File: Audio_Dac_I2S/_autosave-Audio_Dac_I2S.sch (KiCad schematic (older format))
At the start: 35 parts

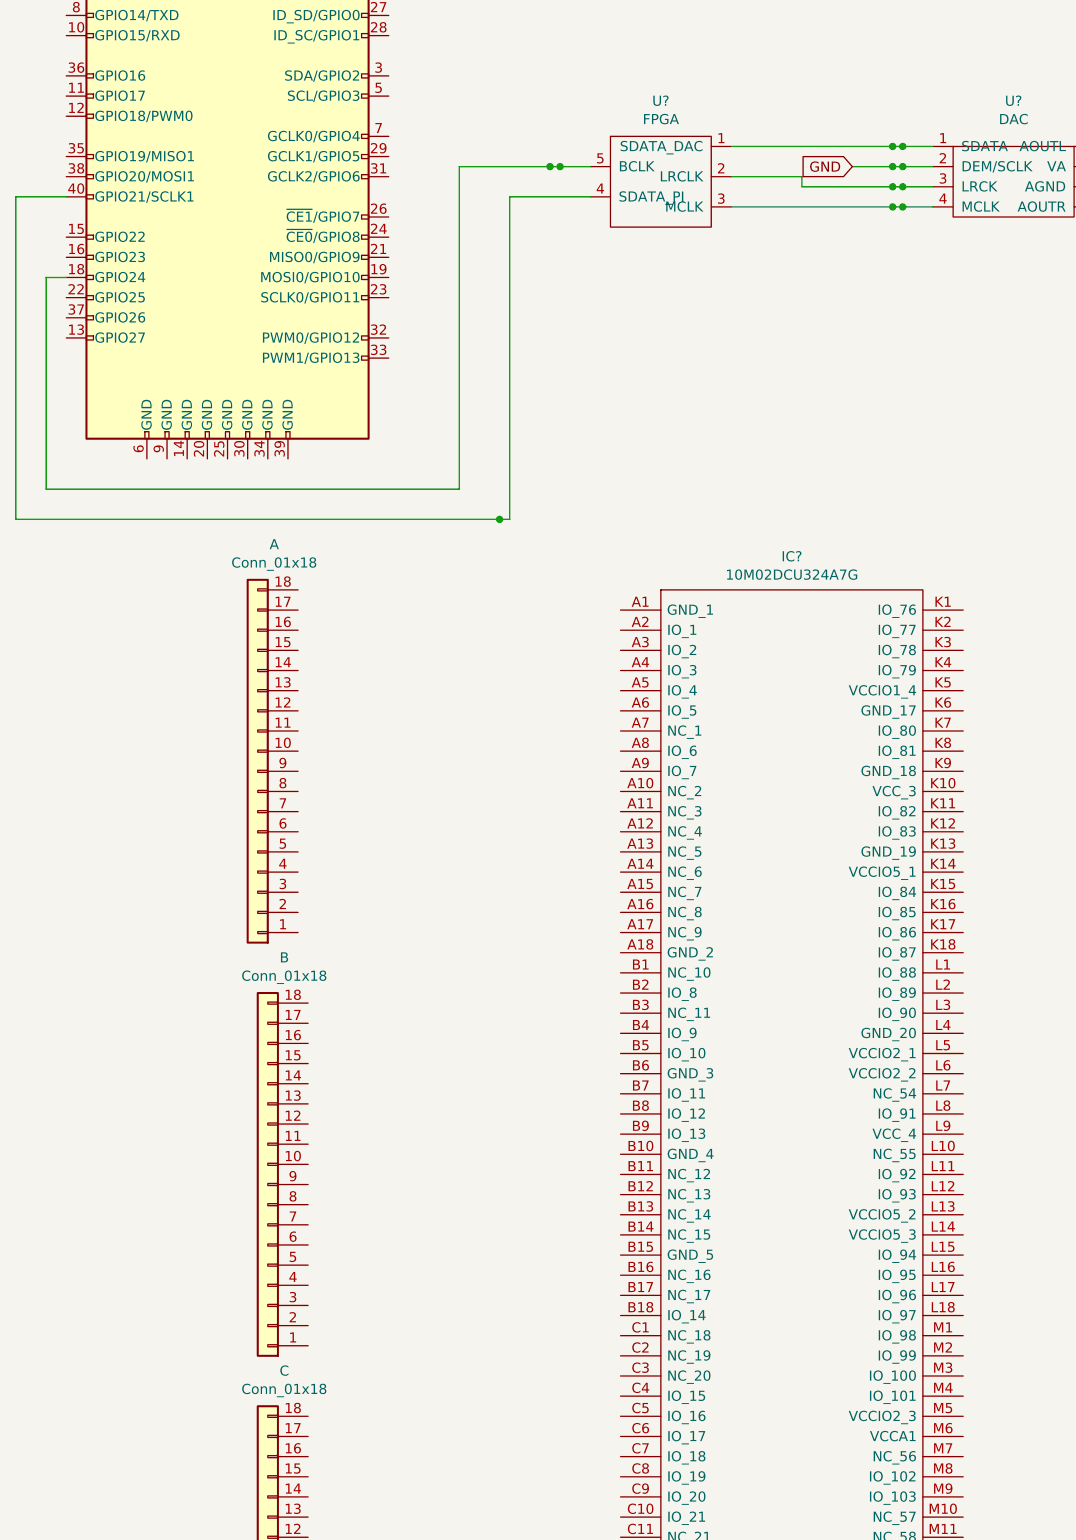
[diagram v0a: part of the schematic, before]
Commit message: updated schematics and footprints
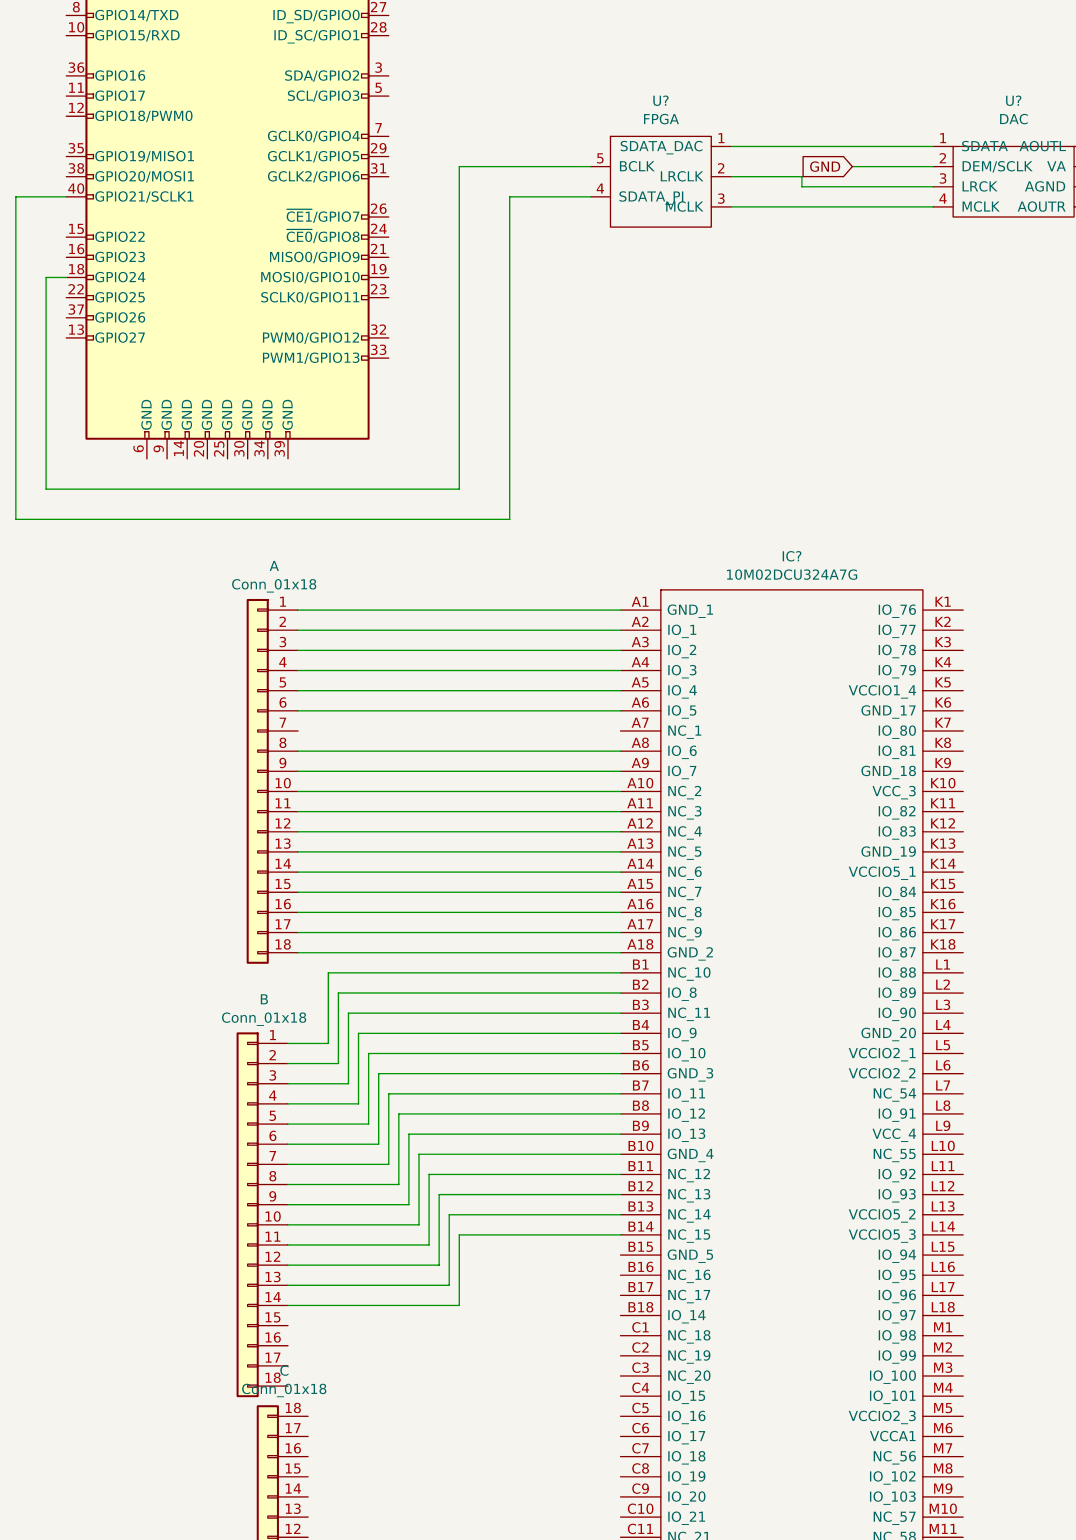
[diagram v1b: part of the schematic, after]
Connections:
- net at IC?.A1 (GND_1): now also A.1 (Pin_1)
- net at IC?.A10 (NC_2): now also A.10 (Pin_10)
- net at IC?.A11 (NC_3): now also A.11 (Pin_11)
- net at IC?.A12 (NC_4): now also A.12 (Pin_12)
- net at IC?.A13 (NC_5): now also A.13 (Pin_13)
- net at IC?.A14 (NC_6): now also A.14 (Pin_14)
- net at IC?.A15 (NC_7): now also A.15 (Pin_15)
- net at IC?.A16 (NC_8): now also A.16 (Pin_16)
- net at IC?.A17 (NC_9): now also A.17 (Pin_17)
- net at IC?.A18 (GND_2): now also A.18 (Pin_18)
- net at IC?.A2 (IO_1): now also A.2 (Pin_2)
- net at IC?.A3 (IO_2): now also A.3 (Pin_3)
- net at IC?.A4 (IO_3): now also A.4 (Pin_4)
- net at IC?.A5 (IO_4): now also A.5 (Pin_5)
- net at IC?.A6 (IO_5): now also A.6 (Pin_6)
- net at IC?.A8 (IO_6): now also A.8 (Pin_8)
- net at IC?.A9 (IO_7): now also A.9 (Pin_9)
- net at IC?.B1 (NC_10): now also B.1 (Pin_1)
- net at IC?.B10 (GND_4): now also B.10 (Pin_10)
- net at IC?.B11 (NC_12): now also B.11 (Pin_11)
- net at IC?.B12 (NC_13): now also B.12 (Pin_12)
- net at IC?.B13 (NC_14): now also B.13 (Pin_13)
- net at IC?.B14 (NC_15): now also B.14 (Pin_14)
- net at IC?.B2 (IO_8): now also B.2 (Pin_2)
- net at IC?.B3 (NC_11): now also B.3 (Pin_3)
- net at IC?.B4 (IO_9): now also B.4 (Pin_4)
- net at IC?.B5 (IO_10): now also B.5 (Pin_5)
- net at IC?.B6 (GND_3): now also B.6 (Pin_6)
- net at IC?.B7 (IO_11): now also B.7 (Pin_7)
- net at IC?.B8 (IO_12): now also B.8 (Pin_8)
- net at IC?.B9 (IO_13): now also B.9 (Pin_9)
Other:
- moved on the sheet: A, B
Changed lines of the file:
@@
 Text GLabel 4900 3400 0    50   Input ~ 0
 GND
-Wire Wire Line
-	5300 3400 5150 3400
 $Comp
 L CustomLib:FPGA U?
@@
 $EndComp
 Wire Wire Line
-	4300 3600 5100 3600
-Wire Wire Line
 	4300 3450 4650 3450
 Wire Wire Line
 	4650 3450 4650 3500
-Wire Wire Line
-	4650 3500 5100 3500
-Wire Wire Line
-	4300 3300 5100 3300
 $Comp
 L Connector:Raspberry_Pi_2_3 J?
@@
 	750  3550 750  5150
 Wire Wire Line
-	750  5150 3150 5150
-Wire Wire Line
 	3200 5150 3200 3550
 Wire Wire Line
@@
 Wire Wire Line
 	2950 5000 2950 3400
-Wire Wire Line
-	2950 3400 3400 3400
 Wire Wire Line
 	8100 4800 9200 4800
@@
 	1    0    0    -1
 $EndComp
-Connection ~ 3450 3400
-Wire Wire Line
-	3450 3400 3600 3400
-Connection ~ 5150 3300
-Wire Wire Line
-	5150 3300 5300 3300
-Connection ~ 5150 3400
-Wire Wire Line
-	5150 3400 5100 3400
-Connection ~ 5150 3500
-Wire Wire Line
-	5150 3500 5300 3500
-Connection ~ 5150 3600
-Wire Wire Line
-	5150 3600 5300 3600
-Connection ~ 3400 3400
-Wire Wire Line
-	3400 3400 3450 3400
-Connection ~ 5100 3300
-Wire Wire Line
-	5100 3300 5150 3300
-Connection ~ 5100 3400
-Wire Wire Line
-	5100 3400 4900 3400
-Connection ~ 5100 3500
-Wire Wire Line
-	5100 3500 5150 3500
-Connection ~ 5100 3600
-Wire Wire Line
-	5100 3600 5150 3600
-Connection ~ 3150 5150
-Wire Wire Line
-	3150 5150 3200 5150
-$Comp
-L Connector_Generic:Conn_01x18 A
-U 1 1 6195A7F2
-P 1950 6400
-F 0 "A" H 1868 5275 50  0000 C CNN
-F 1 "Conn_01x18" H 1868 5366 50  0000 C CNN
-F 2 "" H 1950 6400 50  0001 C CNN
-F 3 "~" H 1950 6400 50  0001 C CNN
-	1    1950 6400
-	-1   0    0    1
-$EndComp
 $Comp
 L Connector_Generic:Conn_01x18 B
 U 1 1 6195C231
-P 2000 8450
-F 0 "B" H 1918 7325 50  0000 C CNN
-F 1 "Conn_01x18" H 1918 7416 50  0000 C CNN
-F 2 "" H 2000 8450 50  0001 C CNN
-F 3 "~" H 2000 8450 50  0001 C CNN
-	1    2000 8450
-	-1   0    0    1
+P 1900 8550
+F 0 "B" H 1818 9567 50  0000 C CNN
+F 1 "Conn_01x18" H 1818 9476 50  0000 C CNN
+F 2 "" H 1900 8550 50  0001 C CNN
+F 3 "~" H 1900 8550 50  0001 C CNN
+	1    1900 8550
+	-1   0    0    -1
 $EndComp
 $Comp
@@
 	1    0    0    -1
 $EndComp
+$Comp
+L Connector_Generic:Conn_01x18 A
+U 1 1 6195A7F2
+P 1950 6400
+F 0 "A" H 1868 7417 50  0000 C CNN
+F 1 "Conn_01x18" H 1868 7326 50  0000 C CNN
+F 2 "" H 1950 6400 50  0001 C CNN
+F 3 "~" H 1950 6400 50  0001 C CNN
+	1    1950 6400
+	-1   0    0    -1
+$EndComp
+Wire Wire Line
+	2950 3400 3600 3400
+Wire Wire Line
+	750  5150 3200 5150
+Wire Wire Line
+	4300 3300 5300 3300
+Wire Wire Line
+	4650 3500 5300 3500
+Wire Wire Line
+	4300 3600 5300 3600
+Wire Wire Line
+	4900 3400 5300 3400
+Wire Wire Line
+	2150 5600 3750 5600
+Wire Wire Line
+	3750 5700 2150 5700
+Wire Wire Line
+	2150 5800 3750 5800
+Wire Wire Line
+	3750 5900 2150 5900
+Wire Wire Line
+	2150 6000 3750 6000
+Wire Wire Line
+	3750 6100 2150 6100
+Wire Wire Line
+	2150 6300 3750 6300
+Wire Wire Line
+	2150 6400 3750 6400
+Wire Wire Line
+	3750 6500 2150 6500
+Wire Wire Line
+	2150 6600 3750 6600
+Wire Wire Line
+	3750 6700 2150 6700
+Wire Wire Line
+	2150 6800 3750 6800
+Wire Wire Line
+	3750 6900 2150 6900
+Wire Wire Line
+	2150 7000 3750 7000
+Wire Wire Line
+	3750 7100 2150 7100
+Wire Wire Line
+	2150 7200 3750 7200
+Wire Wire Line
+	3750 7300 2150 7300
+Wire Wire Line
+	2100 7750 2300 7750
+Wire Wire Line
+	2300 7750 2300 7400
+Wire Wire Line
+	2300 7400 3750 7400
+Wire Wire Line
+	3750 7500 2350 7500
+Wire Wire Line
+	2350 7500 2350 7850
+Wire Wire Line
+	2350 7850 2100 7850
+Wire Wire Line
+	2100 7950 2400 7950
+Wire Wire Line
+	2400 7950 2400 7600
+Wire Wire Line
+	2400 7600 3750 7600
+Wire Wire Line
+	3750 7700 2450 7700
+Wire Wire Line
+	2450 7700 2450 8050
+Wire Wire Line
+	2450 8050 2100 8050
+Wire Wire Line
+	2100 8150 2500 8150
+Wire Wire Line
+	2500 8150 2500 7800
+Wire Wire Line
+	2500 7800 3750 7800
+Wire Wire Line
+	3750 7900 2550 7900
+Wire Wire Line
+	2550 7900 2550 8250
+Wire Wire Line
+	2550 8250 2100 8250
+Wire Wire Line
+	2100 8350 2600 8350
+Wire Wire Line
+	2600 8350 2600 8000
+Wire Wire Line
+	2600 8000 3750 8000
+Wire Wire Line
+	3750 8100 2650 8100
+Wire Wire Line
+	2650 8100 2650 8450
+Wire Wire Line
+	2650 8450 2100 8450
+Wire Wire Line
+	3750 8200 2700 8200
+Wire Wire Line
+	2700 8200 2700 8550
+Wire Wire Line
+	2700 8550 2100 8550
+Wire Wire Line
+	2100 8650 2750 8650
+Wire Wire Line
+	2750 8650 2750 8300
+Wire Wire Line
+	2750 8300 3750 8300
+Wire Wire Line
+	3750 8400 2800 8400
+Wire Wire Line
+	2800 8400 2800 8750
+Wire Wire Line
+	2800 8750 2100 8750
+Wire Wire Line
+	2100 8850 2850 8850
+Wire Wire Line
+	2850 8850 2850 8500
+Wire Wire Line
+	2850 8500 3750 8500
+Wire Wire Line
+	3750 8600 2900 8600
+Wire Wire Line
+	2900 8600 2900 8950
+Wire Wire Line
+	2900 8950 2100 8950
+Wire Wire Line
+	2100 9050 2950 9050
+Wire Wire Line
+	2950 9050 2950 8700
+Wire Wire Line
+	2950 8700 3750 8700
 $EndSCHEMATC
